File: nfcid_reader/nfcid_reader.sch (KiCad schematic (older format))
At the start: 18 parts, among them J1 BARREL_JACK, J2 ESP32_LEFT, J3 ESP32_RIGHT, J4 PN532, Q1 Q_PMOS_GSD, U1 MCP73832-2-OT, U2 NCP1117-3.3_SOT223

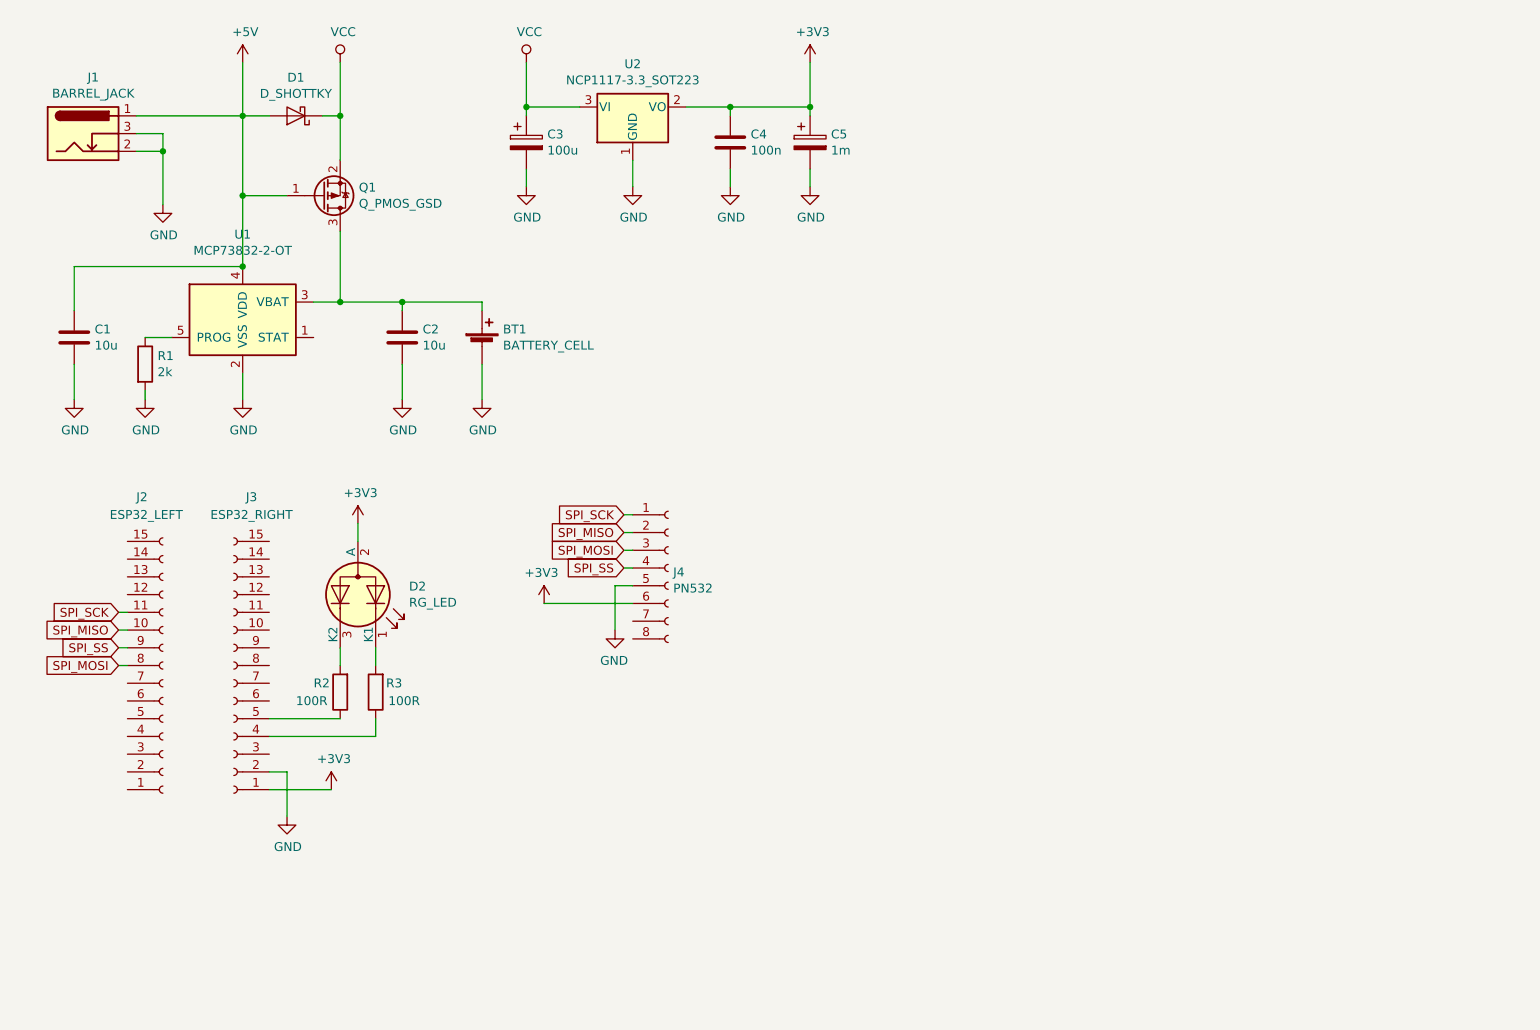
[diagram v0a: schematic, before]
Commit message: Scheme update. Footprint assignation started.
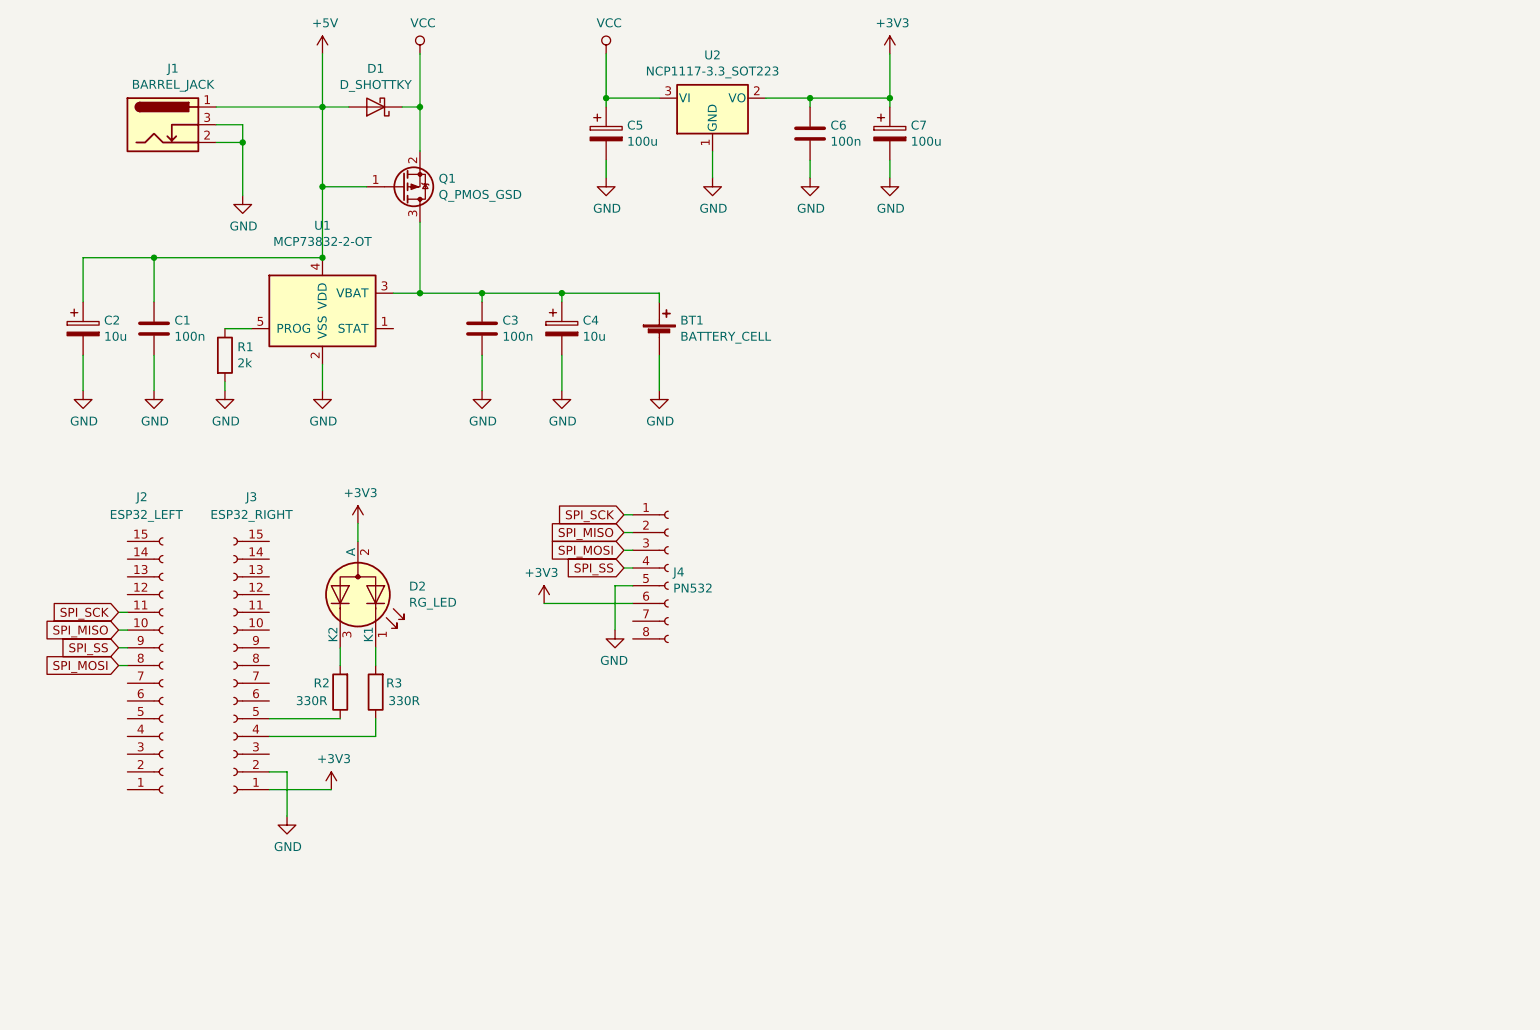
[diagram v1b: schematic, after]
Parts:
- added C2, C4: 10u, Capacitor_THT:CP_Radial_D6.3mm_P2.50mm, symbol Device:CP
- C1: value 10u -> 100n; footprint (none) -> Capacitor_THT:C_Disc_D3.0mm_W1.6mm_P2.50mm
- C3: renamed from C2; value 10u -> 100n; footprint (none) -> Capacitor_THT:C_Disc_D3.0mm_W1.6mm_P2.50mm
- C5: renamed from C3; footprint (none) -> Capacitor_THT:CP_Radial_D6.3mm_P2.50mm
- C6: renamed from C4; footprint (none) -> Capacitor_THT:C_Disc_D3.0mm_W1.6mm_P2.50mm
- C7: renamed from C5; value 1m -> 100u; footprint (none) -> Capacitor_THT:CP_Radial_D6.3mm_P2.50mm
- D1: footprint (none) -> Diode_THT:D_5KPW_P12.70mm_Horizontal
- D2: footprint (none) -> LED_THT:LED_D5.0mm-3
- J1: footprint (none) -> Connector_BarrelJack:BarrelJack_CUI_PJ-063AH_Horizontal
- J2, J3: footprint (none) -> Connector_PinSocket_2.54mm:PinSocket_1x15_P2.54mm_Vertical
- J4, Q1: footprint (none) -> Connector_PinSocket_2.54mm:PinSocket_1x08_P2.54mm_Horizontal
- R1: footprint (none) -> Resistor_THT:R_Axial_DIN0204_L3.6mm_D1.6mm_P7.62mm_Horizontal
- R2: value 100R -> 330R; footprint (none) -> Resistor_THT:R_Axial_DIN0204_L3.6mm_D1.6mm_P7.62mm_Horizontal
- R3: renamed from 100R; value R3 -> 330R; footprint (none) -> Resistor_THT:R_Axial_DIN0204_L3.6mm_D1.6mm_P7.62mm_Horizontal
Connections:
- net +5V: now also C2.1
- net GND: now also C2.2, C4.2
- net at BT1.1 (+), C3.1, Q1.3 (D)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: now also C4.1
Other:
- moved on the sheet: BT1, C1, C3, C5, C6, C7, D1, J1, Q1, R1, U1, U2

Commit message: First draft. Problems to be solved: thick via, bridge.
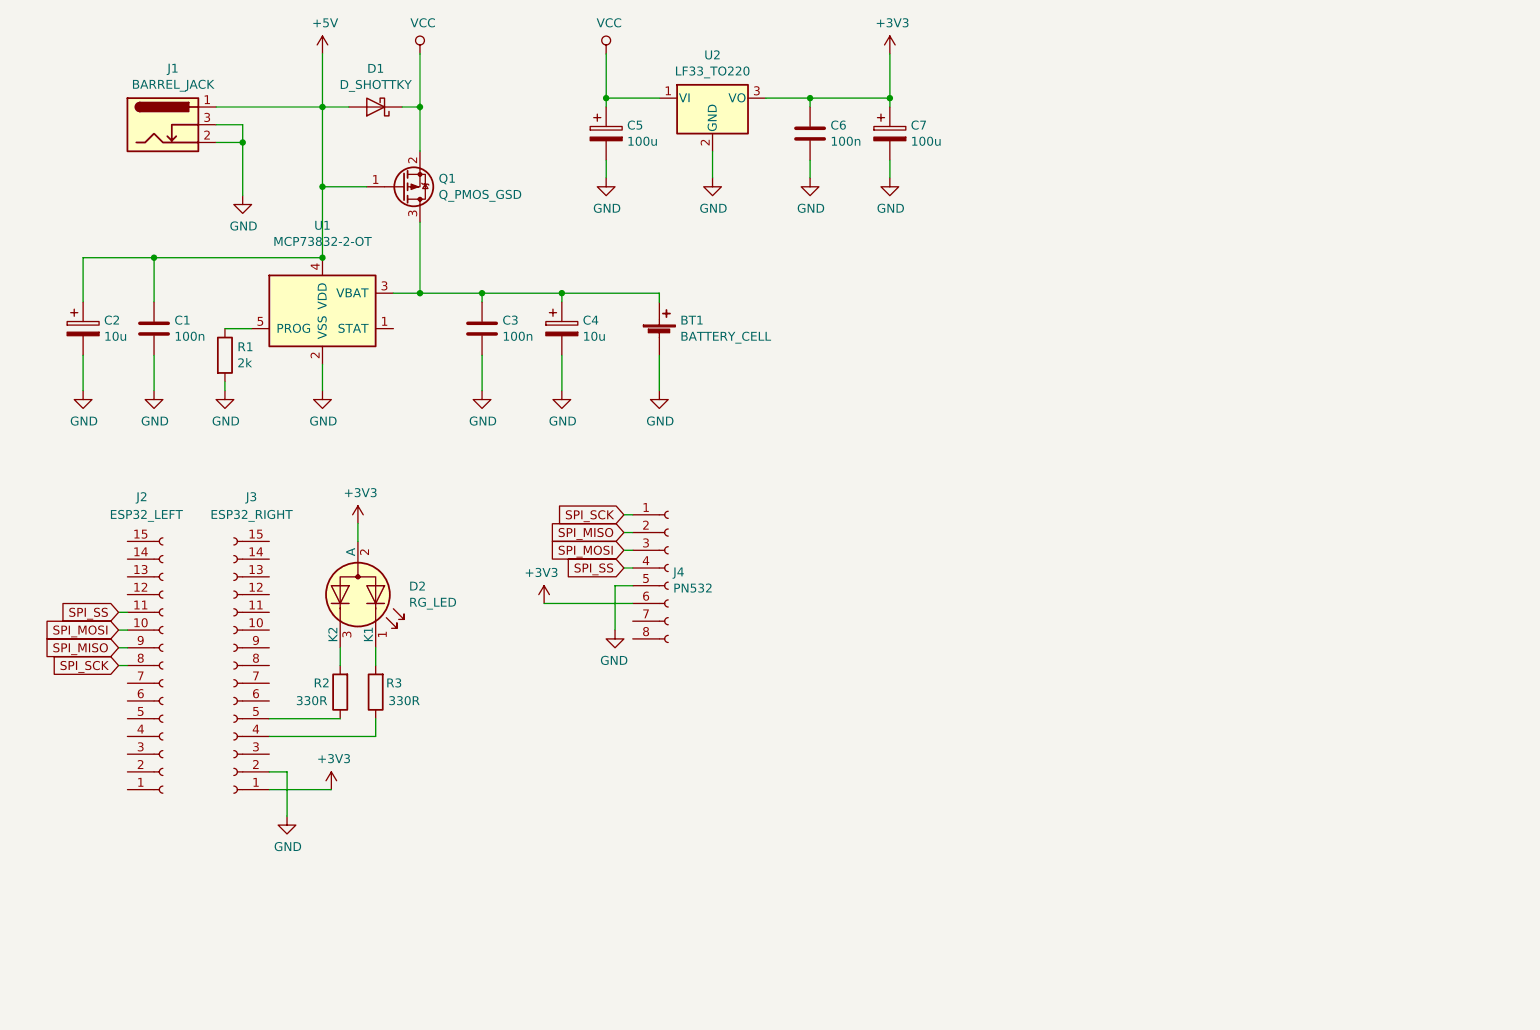
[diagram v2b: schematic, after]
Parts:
- removed U2: NCP1117-3.3_SOT223, Package_TO_SOT_SMD:SOT-223-3_TabPin2, symbol Regulator_Linear:NCP1117-3.3_SOT223
- added U2: LF33_TO220, Package_TO_SOT_THT:TO-220-3_Vertical, symbol Regulator_Linear:LF33_TO220
- BT1: footprint (none) -> TestPoint:TestPoint_2Pads_Pitch2.54mm_Drill0.8mm
- D1: footprint Diode_THT:D_5KPW_P12.70mm_Horizontal -> Diode_THT:D_A-405_P7.62mm_Horizontal
- J1: footprint Connector_BarrelJack:BarrelJack_CUI_PJ-063AH_Horizontal -> Connector_BarrelJack:BarrelJack_Horizontal
- Q1: footprint Connector_PinSocket_2.54mm:PinSocket_1x08_P2.54mm_Horizontal -> Package_TO_SOT_SMD:SOT-23_Handsoldering
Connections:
- net +3V3: now also U2.3 (VO)
- net GND: now also U2.2 (GND)
- net SPI_MISO: now also J2.9 (Pin_9); no longer J2.10 (Pin_10)
- net SPI_MOSI: now also J2.10 (Pin_10); no longer J2.8 (Pin_8)
- net SPI_SCK: now also J2.8 (Pin_8); no longer J2.11 (Pin_11)
- net SPI_SS: now also J2.11 (Pin_11); no longer J2.9 (Pin_9)
- net VCC: now also U2.1 (VI)
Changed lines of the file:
@@
 F 0 "J1" H 1507 1567 50  0000 C CNN
 F 1 "BARREL_JACK" H 1507 1476 50  0000 C CNN
-F 2 "Connector_BarrelJack:BarrelJack_CUI_PJ-063AH_Horizontal" H 1500 1210 50  0001 C CNN
+F 2 "Connector_BarrelJack:BarrelJack_Horizontal" H 1500 1210 50  0001 C CNN
 F 3 "~" H 1500 1210 50  0001 C CNN
 	1    1450 1250
@@
 F 0 "Q1" H 3005 1554 50  0000 L CNN
 F 1 "Q_PMOS_GSD" H 3005 1645 50  0000 L CNN
-F 2 "Connector_PinSocket_2.54mm:PinSocket_1x08_P2.54mm_Horizontal" H 3000 1700 50  0001 C CNN
+F 2 "Package_TO_SOT_SMD:SOT-23_Handsoldering" H 3000 1700 50  0001 C CNN
 F 3 "~" H 2800 1600 50  0001 C CNN
 	1    2800 1600
@@
 F 0 "BT1" H 4368 2546 50  0000 L CNN
 F 1 "BATTERY_CELL" H 4368 2455 50  0000 L CNN
-F 2 "" V 4250 2510 50  0001 C CNN
+F 2 "TestPoint:TestPoint_2Pads_Pitch2.54mm_Drill0.8mm" V 4250 2510 50  0001 C CNN
 F 3 "~" V 4250 2510 50  0001 C CNN
 	1    4250 2450
@@
 F 0 "D1" H 2650 934 50  0000 C CNN
 F 1 "D_SHOTTKY" H 2650 1025 50  0000 C CNN
-F 2 "Diode_THT:D_5KPW_P12.70mm_Horizontal" H 2650 1150 50  0001 C CNN
+F 2 "Diode_THT:D_A-405_P7.62mm_Horizontal" H 2650 1150 50  0001 C CNN
 F 3 "~" H 2650 1150 50  0001 C CNN
 	1    2650 1150
@@
 	2900 850  2900 1150
 Connection ~ 2900 1150
-$Comp
-L Regulator_Linear:NCP1117-3.3_SOT223 U2
-U 1 1 5E95D4C3
-P 4550 1100
-F 0 "U2" H 4550 1342 50  0000 C CNN
-F 1 "NCP1117-3.3_SOT223" H 4550 1251 50  0000 C CNN
-F 2 "Package_TO_SOT_SMD:SOT-223-3_TabPin2" H 4550 1300 50  0001 C CNN
-F 3 "http://www.onsemi.com/pub_link/Collateral/NCP1117-D.PDF" H 4650 850 50  0001 C CNN
-	1    4550 1100
-	1    0    0    -1
-$EndComp
 $Comp
 L Device:CP C5
@@
 	1    0    0    1
 $EndComp
+Text GLabel 1200 4300 0    50   Input ~ 0
+SPI_SCK
+Text GLabel 1200 4200 0    50   Input ~ 0
+SPI_MISO
+Text GLabel 1200 4100 0    50   Input ~ 0
+SPI_MOSI
 Text GLabel 1200 4000 0    50   Input ~ 0
-SPI_SCK
-Text GLabel 1200 4100 0    50   Input ~ 0
-SPI_MISO
-Text GLabel 1200 4300 0    50   Input ~ 0
-SPI_MOSI
-Text GLabel 1200 4200 0    50   Input ~ 0
 SPI_SS
 Wire Wire Line
@@
 	1000 2000 1400 2000
 Connection ~ 1400 2000
+$Comp
+L Regulator_Linear:LF33_TO220 U2
+U 1 1 5E9B4988
+P 4550 1100
+F 0 "U2" H 4550 1342 50  0000 C CNN
+F 1 "LF33_TO220" H 4550 1251 50  0000 C CNN
+F 2 "Package_TO_SOT_THT:TO-220-3_Vertical" H 4550 1325 50  0001 C CIN
+F 3 "http://www.st.com/content/ccc/resource/technical/document/datasheet/c4/0e/7e/2a/be/bc/4c/bd/CD00000546.pdf/files/CD00000546.pdf/jcr:content/translations/en.CD00000546.pdf" H 4550 1050 50  0001 C CNN
+	1    4550 1100
+	1    0    0    -1
+$EndComp
 $EndSCHEMATC

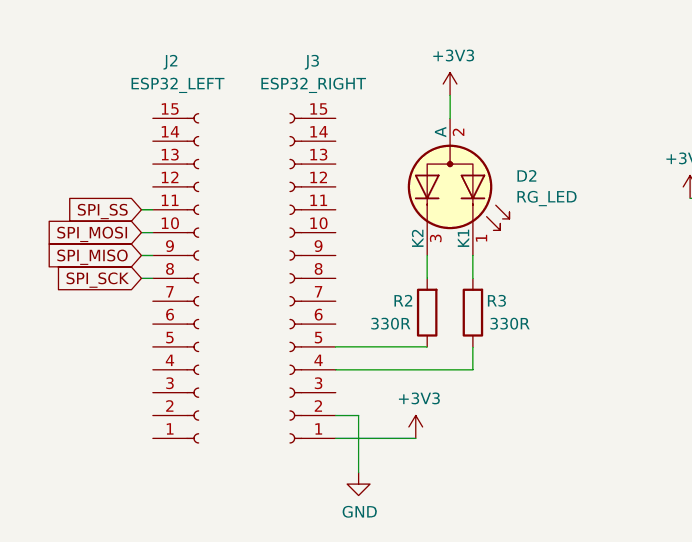
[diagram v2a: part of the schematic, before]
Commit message: Fixed thick track, ESP orentation. Added bridge, edge cuts.
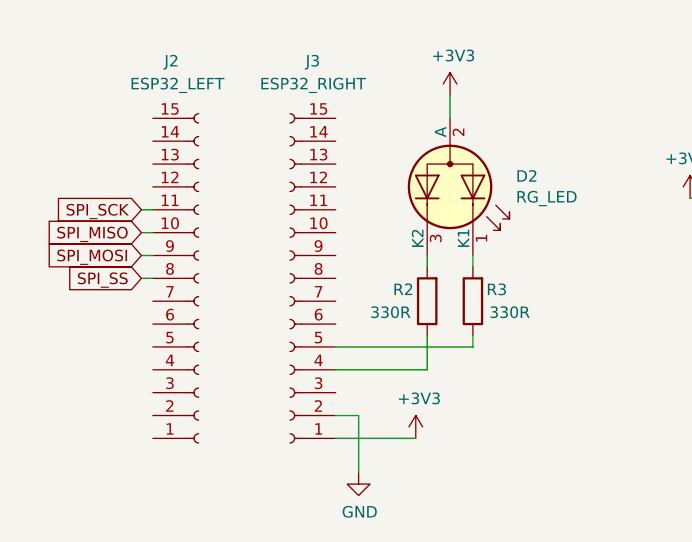
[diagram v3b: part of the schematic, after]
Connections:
- net SPI_MISO: now also J2.10 (Pin_10); no longer J2.9 (Pin_9)
- net SPI_MOSI: now also J2.9 (Pin_9); no longer J2.10 (Pin_10)
- net SPI_SCK: now also J2.11 (Pin_11); no longer J2.8 (Pin_8)
- net SPI_SS: now also J2.8 (Pin_8); no longer J2.11 (Pin_11)
- net at J3.4 (Pin_4): now also R2.1; no longer R3.1
- net at J3.5 (Pin_5): now also R3.1; no longer R2.1
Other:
- moved on the sheet: R2, R3
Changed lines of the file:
@@
 	1    0    0    1
 $EndComp
-Text GLabel 1200 4300 0    50   Input ~ 0
-SPI_SCK
-Text GLabel 1200 4200 0    50   Input ~ 0
-SPI_MISO
-Text GLabel 1200 4100 0    50   Input ~ 0
-SPI_MOSI
-Text GLabel 1200 4000 0    50   Input ~ 0
-SPI_SS
 Wire Wire Line
 	1200 4000 1250 4000
@@
 Wire Wire Line
 	1200 4300 1250 4300
-$Comp
-L Device:R R3
-U 1 1 5E9AE8E2
-P 2650 4450
-F 0 "R3" H 2500 4400 50  0000 L CNN
-F 1 "330R" H 2400 4500 50  0000 L CNN
-F 2 "Resistor_THT:R_Axial_DIN0204_L3.6mm_D1.6mm_P7.62mm_Horizontal" V 2580 4450 50  0001 C CNN
-F 3 "~" H 2650 4450 50  0001 C CNN
-	1    2650 4450
-	-1   0    0    1
-$EndComp
-$Comp
-L Device:R R2
-U 1 1 5E9B3809
-P 2450 4450
-F 0 "R2" H 2600 4400 50  0000 R CNN
-F 1 "330R" H 2700 4500 50  0000 R CNN
-F 2 "Resistor_THT:R_Axial_DIN0204_L3.6mm_D1.6mm_P7.62mm_Horizontal" V 2380 4450 50  0001 C CNN
-F 3 "~" H 2450 4450 50  0001 C CNN
-	1    2450 4450
-	-1   0    0    1
-$EndComp
-Wire Wire Line
-	2650 4300 2650 4200
-Wire Wire Line
-	2450 4300 2450 4200
-$Comp
-L power:+3V3 #PWR0119
-U 1 1 5E9B960A
-P 2550 3500
-F 0 "#PWR0119" H 2550 3350 50  0001 C CNN
-F 1 "+3V3" H 2565 3673 50  0000 C CNN
-F 2 "" H 2550 3500 50  0001 C CNN
-F 3 "" H 2550 3500 50  0001 C CNN
-	1    2550 3500
-	1    0    0    -1
-$EndComp
-Wire Wire Line
-	2050 4600 2450 4600
-Wire Wire Line
-	2050 4700 2650 4700
-Wire Wire Line
-	2650 4700 2650 4600
-Wire Wire Line
-	2550 3500 2550 3600
-$Comp
-L Device:LED_Dual_CAC D2
-U 1 1 5E9CBB87
-P 2550 3900
-F 0 "D2" V 2504 4188 50  0000 L CNN
-F 1 "RG_LED" V 2595 4188 50  0000 L CNN
-F 2 "LED_THT:LED_D5.0mm-3" H 2600 3900 50  0001 C CNN
-F 3 "~" H 2600 3900 50  0001 C CNN
-	1    2550 3900
-	0    1    1    0
-$EndComp
 $Comp
 L Device:CP C4
@@
 	1    0    0    -1
 $EndComp
+$Comp
+L Device:R R3
+U 1 1 5E9AE8E2
+P 2650 4400
+F 0 "R3" H 2500 4350 50  0000 L CNN
+F 1 "330R" H 2400 4450 50  0000 L CNN
+F 2 "Resistor_THT:R_Axial_DIN0204_L3.6mm_D1.6mm_P7.62mm_Horizontal" V 2580 4400 50  0001 C CNN
+F 3 "~" H 2650 4400 50  0001 C CNN
+	1    2650 4400
+	-1   0    0    1
+$EndComp
+Text GLabel 1200 4100 0    50   Input ~ 0
+SPI_MISO
+Text GLabel 1200 4200 0    50   Input ~ 0
+SPI_MOSI
+Text GLabel 1200 4300 0    50   Input ~ 0
+SPI_SS
+Text GLabel 1200 4000 0    50   Input ~ 0
+SPI_SCK
+Wire Wire Line
+	2550 3500 2550 3600
+$Comp
+L power:+3V3 #PWR0119
+U 1 1 5E9B960A
+P 2550 3500
+F 0 "#PWR0119" H 2550 3350 50  0001 C CNN
+F 1 "+3V3" H 2565 3673 50  0000 C CNN
+F 2 "" H 2550 3500 50  0001 C CNN
+F 3 "" H 2550 3500 50  0001 C CNN
+	1    2550 3500
+	1    0    0    -1
+$EndComp
+$Comp
+L Device:LED_Dual_CAC D2
+U 1 1 5E9CBB87
+P 2550 3900
+F 0 "D2" V 2504 4188 50  0000 L CNN
+F 1 "RG_LED" V 2595 4188 50  0000 L CNN
+F 2 "LED_THT:LED_D5.0mm-3" H 2600 3900 50  0001 C CNN
+F 3 "~" H 2600 3900 50  0001 C CNN
+	1    2550 3900
+	0    1    1    0
+$EndComp
+$Comp
+L Device:R R2
+U 1 1 5E9B3809
+P 2450 4400
+F 0 "R2" H 2600 4350 50  0000 R CNN
+F 1 "330R" H 2700 4450 50  0000 R CNN
+F 2 "Resistor_THT:R_Axial_DIN0204_L3.6mm_D1.6mm_P7.62mm_Horizontal" V 2380 4400 50  0001 C CNN
+F 3 "~" H 2450 4400 50  0001 C CNN
+	1    2450 4400
+	-1   0    0    1
+$EndComp
+Wire Wire Line
+	2450 4200 2450 4250
+Wire Wire Line
+	2650 4200 2650 4250
+Wire Wire Line
+	2650 4550 2650 4600
+Wire Wire Line
+	2650 4600 2050 4600
+Wire Wire Line
+	2450 4550 2450 4700
+Wire Wire Line
+	2450 4700 2050 4700
 $EndSCHEMATC
